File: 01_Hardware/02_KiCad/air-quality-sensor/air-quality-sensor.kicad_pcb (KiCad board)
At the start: 2 copper layers, 90 x 90 mm, 111 parts, among them J1 USB_C_Receptacle_USB2.0_16P, J2 Conn_01x03, J3 Conn_01x04, SW1 SW_SPST, U1 SHT4x, U2 SCD41-D-R2, U4 TPS54302, U5 USBLC6-2SC6, U6 SPA06-003, U7 74AHCT1G125, U8 ESP32-S3-WROOM-1

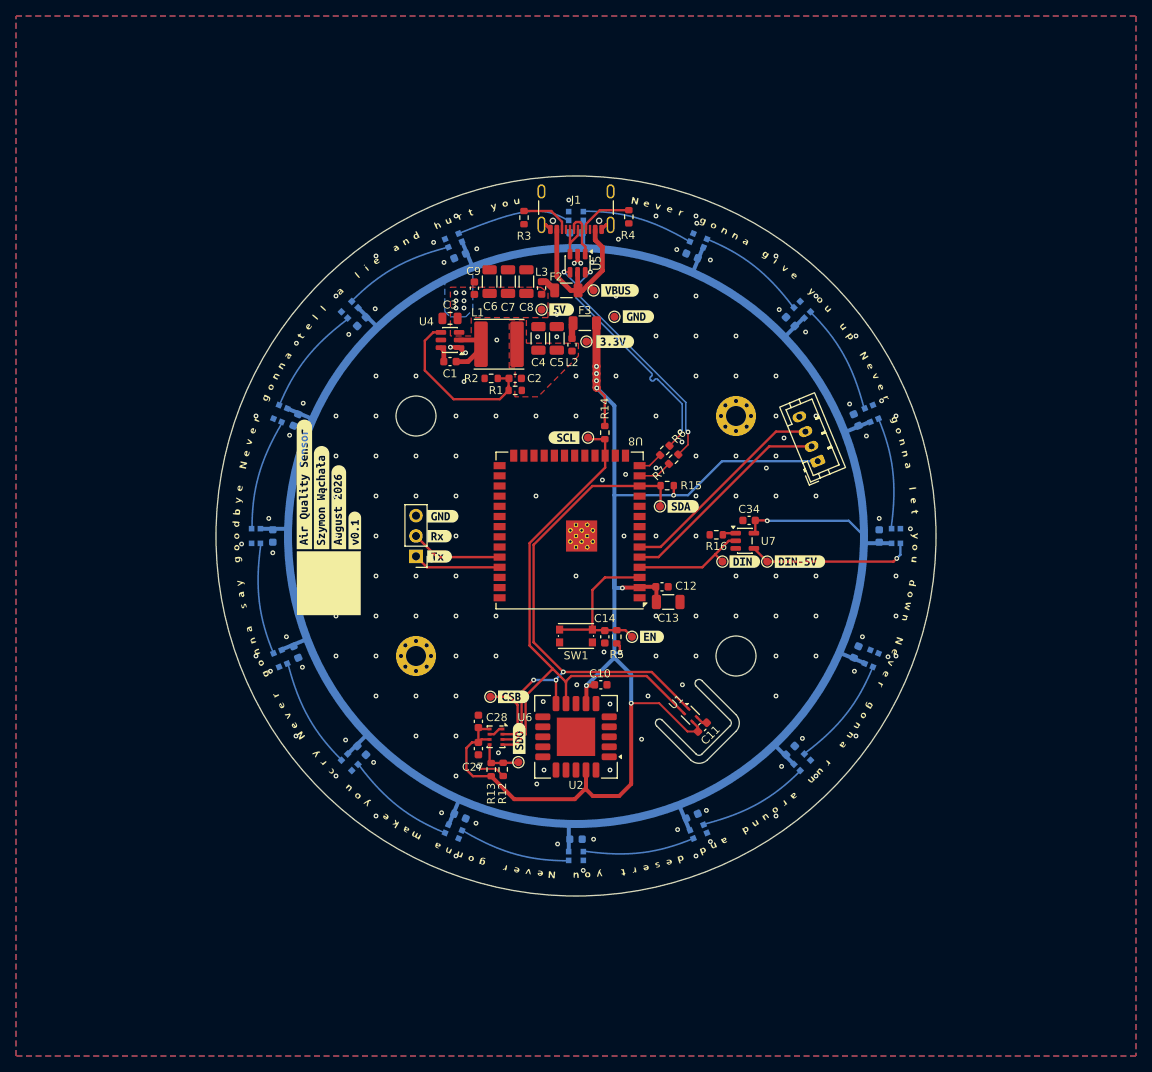
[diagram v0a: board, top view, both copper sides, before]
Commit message: Finished layout of d70mm PCB
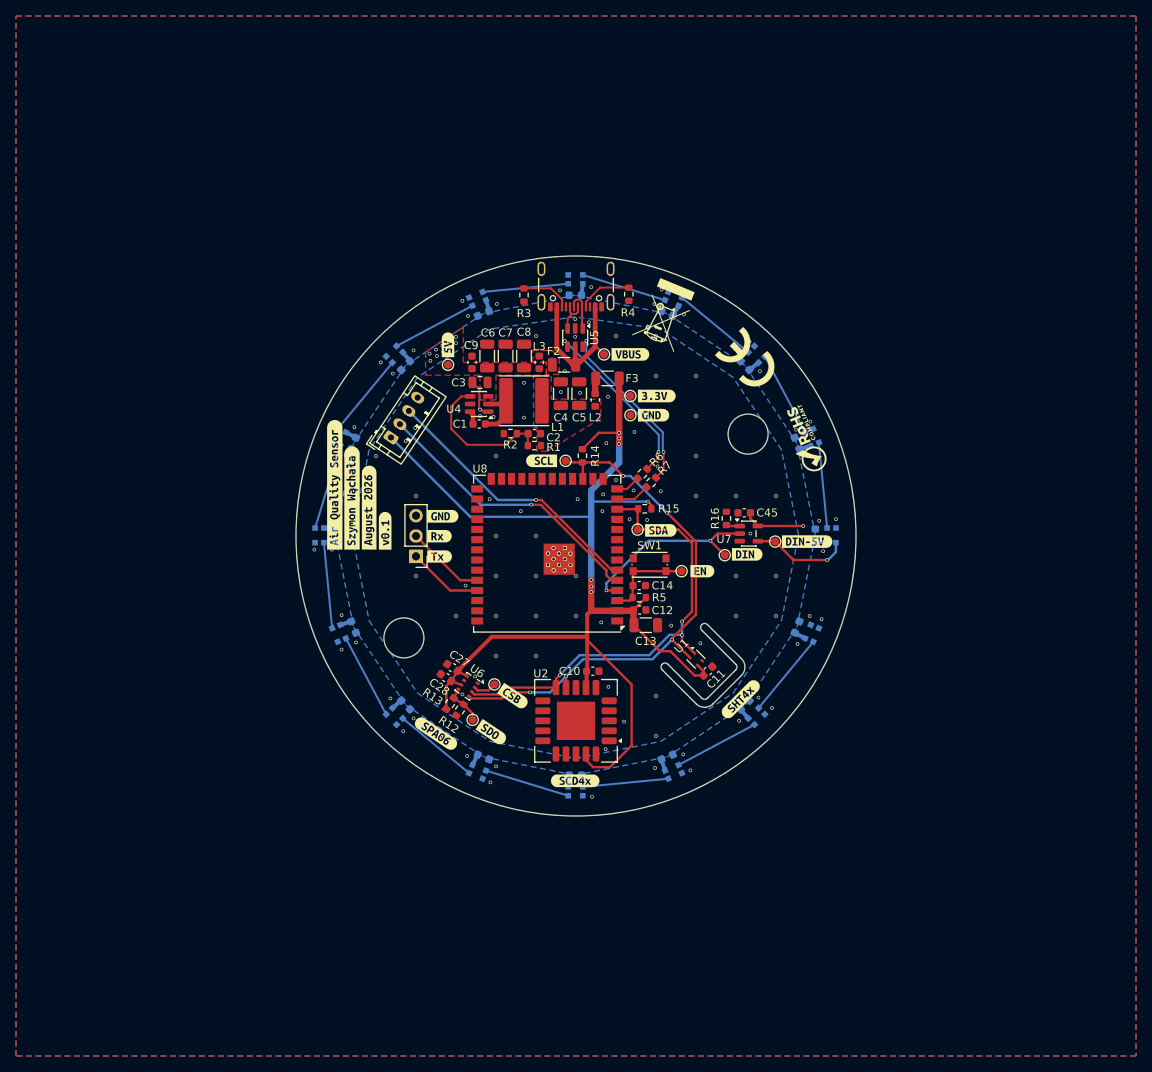
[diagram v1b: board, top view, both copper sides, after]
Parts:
- removed the G*** at (150.0, 100.0)
- removed H2, H4: M2.5, MountingHole:MountingHole_2.5mm_Pad_Via
- added G***: LOGO, LOGO, F.Cu at (161.1, 72.3)
- added G***: LOGO, LOGO, F.Cu at (171.6, 78.1)
- added G***: LOGO, LOGO, F.Cu at (178.5, 87.9)
- added kibuzzard-6A80ED83: G***, kibuzzard-6A80ED83, F.Cu at (170.6, 120.4)
- added kibuzzard-6A80EDA5: G***, kibuzzard-6A80EDA5, F.Cu at (149.9, 130.6)
- added kibuzzard-6A80EDE6: G***, kibuzzard-6A80EDE6, F.Cu at (132.5, 124.7)
- C34: moved to B.Cu
- C45: moved to F.Cu
- moved C35 68.0 mm to (122.2, 88.4), turned to -112.5 degrees
- moved C42 67.8 mm to (179.9, 99.9), turned to 90 degrees
- moved C36 62.9 mm to (128.7, 78.7), turned to -135 degrees
- moved C41 62.7 mm to (177.6, 88.4), turned to 112.5 degrees
- moved J3 53.4 mm to (126.9, 87.7), turned to 56.25 degrees
- moved C34 51.8 mm to (119.9, 99.9), turned to -90 degrees
- moved C33 48.5 mm to (122.2, 111.4), turned to -67.5 degrees
- moved C40 48.2 mm to (171.1, 78.7), turned to 135 degrees
- moved C29 38.3 mm to (161.4, 127.6), turned to 22.5 degrees
- moved C44 38.2 mm to (171.1, 121.1), turned to 45 degrees
- moved C30 38.2 mm to (149.9, 129.9), turned to 0 degrees
- moved H1 27.8 mm to (128.5, 112.7), turned to 67.5 degrees
- moved H3 27.8 mm to (171.5, 87.3), turned to 67.5 degrees
- moved C37 27.0 mm to (138.4, 72.2), turned to -157.5 degrees
- moved C39 26.9 mm to (161.4, 72.2), turned to 157.5 degrees
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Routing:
- net 5V: track 64.1 -> 31.0 mm, vias 7 -> 11
- net /Mcu/SDA: track 73.7 -> 57.8 mm
- net Net-(D14-DOUT): track 0.00 -> 10.7 mm
- net Net-(D10-DOUT): track 0.00 -> 10.7 mm
- net Net-(D15-DOUT): track 0.00 -> 10.7 mm
- net Net-(D17-DOUT): track 0.00 -> 10.7 mm
- net Net-(D5-DOUT): track 0.00 -> 10.7 mm
- net Net-(D13-DOUT): track 0.00 -> 10.7 mm
- net Net-(D10-DIN): track 0.00 -> 10.7 mm
- net Net-(D8-DOUT): track 0.00 -> 10.7 mm
- net Net-(D11-DOUT): track 0.00 -> 10.7 mm
- net Net-(D18-DOUT): track 0.00 -> 10.7 mm
- net Net-(D4-DOUT): track 0.00 -> 10.7 mm
- net Net-(D16-DOUT): track 0.00 -> 10.7 mm
- net Net-(D12-DOUT): track 0.00 -> 10.7 mm
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- added copper zone on F.Cu, net Net-(F2-Pad2)
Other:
- board size 90 x 90 mm -> 70 x 70 mm
